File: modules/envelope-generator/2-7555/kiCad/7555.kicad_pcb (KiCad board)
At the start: 2 copper layers, 81 x 111 mm, 87 parts, among them J1 JUMPER_BUS_GATE, J2 PWR, Q1 BC547, Q2 BC547, Q3 BC547, SW1 SW_SPDT, U1 TL074, U2 ICM7555xP

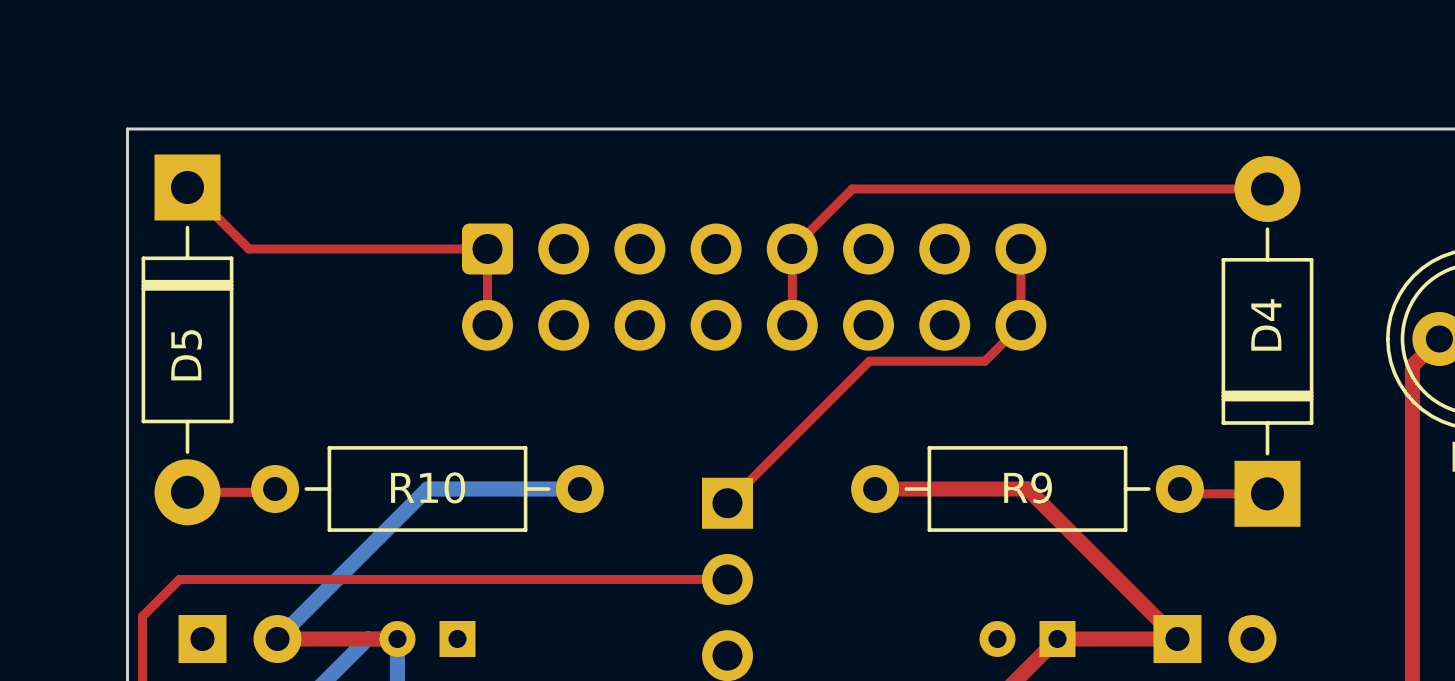
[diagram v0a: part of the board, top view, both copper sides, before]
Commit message: update XFO and 7555 ADSR, update status in readme
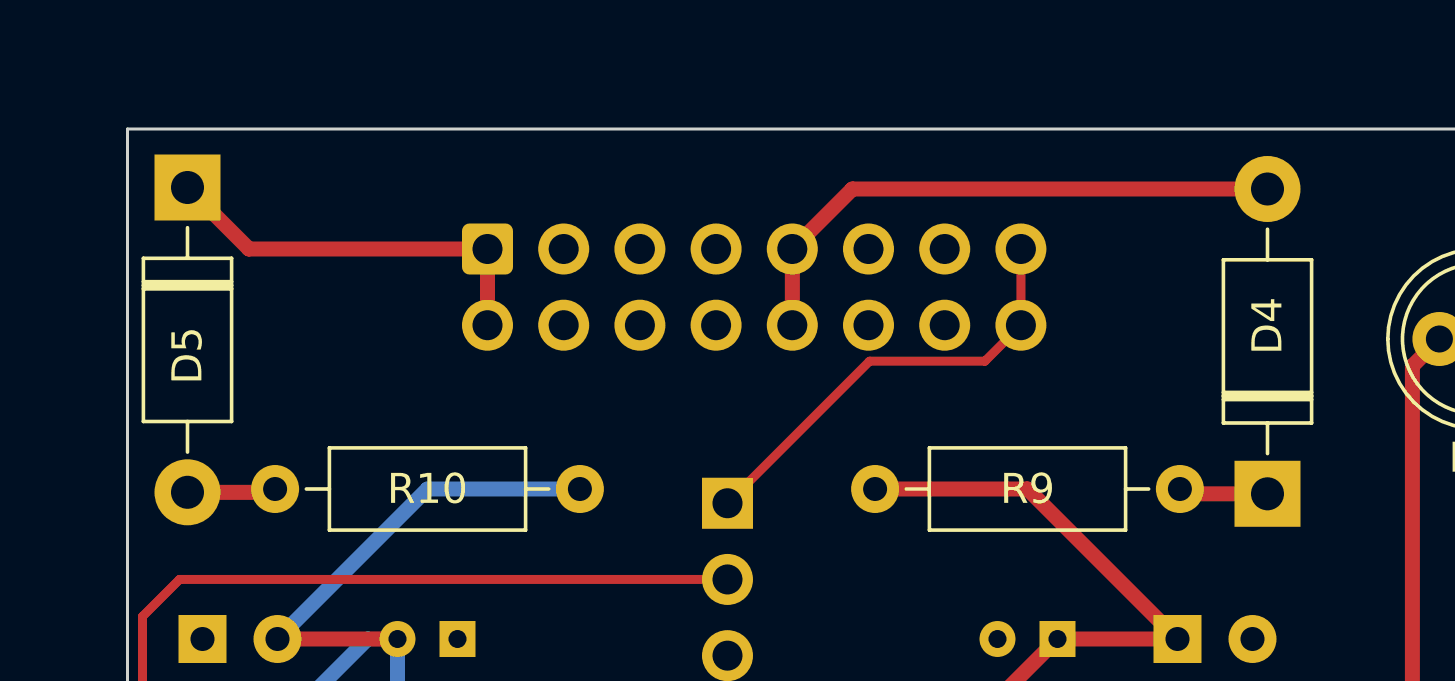
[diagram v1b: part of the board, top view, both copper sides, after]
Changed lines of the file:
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@@
 		(start 62 56.54)
 		(end 62 54)
-		(width 0.3)
+		(width 0.5)
 		(layer "F.Cu")
 		(net 10)
@@
 		(start 54.05 54)
 		(end 52 51.95)
-		(width 0.3)
+		(width 0.5)
 		(layer "F.Cu")
 		(net 10)
@@
 		(start 62 54)
 		(end 54.05 54)
-		(width 0.3)
+		(width 0.5)
 		(layer "F.Cu")
 		(net 10)
@@
 		(start 54.81 62.11)
 		(end 54.92 62)
-		(width 0.3)
+		(width 0.5)
 		(layer "F.Cu")
 		(net 11)
@@
 		(start 52 62.11)
 		(end 54.81 62.11)
-		(width 0.3)
+		(width 0.5)
 		(layer "F.Cu")
 		(net 11)
@@
 		(start 72.16 54)
 		(end 74.16 52)
-		(width 0.3)
+		(width 0.5)
 		(layer "F.Cu")
 		(net 52)
@@
 		(start 72.16 56.54)
 		(end 72.16 54)
-		(width 0.3)
+		(width 0.5)
 		(layer "F.Cu")
 		(net 52)
@@
 		(start 74.16 52)
 		(end 88 52)
-		(width 0.3)
+		(width 0.5)
 		(layer "F.Cu")
 		(net 52)
@@
 		(start 88 62.16)
 		(end 85.24 62.16)
-		(width 0.3)
+		(width 0.5)
 		(layer "F.Cu")
 		(net 53)
@@
 		(start 85.24 62.16)
 		(end 85.08 62)
-		(width 0.3)
+		(width 0.5)
 		(layer "F.Cu")
 		(net 53)

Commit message: update components, PCB 3320 and design
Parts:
- added H15: PinHeader_01x02, Synth:PinSocket_1x02_P2.54mm_Vertical, F.Cu at (53.0, 120.0)
- added H16: PinSocket_01x02, Synth:PinHeader_1x02_P2.54mm_Vertical, B.Cu at (94.0, 120.0)
- C10, C9: moved to B.Cu
- moved C9 68.9 mm to (52.5, 131.2)
- moved C10 51.9 mm to (52.5, 125.0), turned to 0 degrees
- moved TP11 14.8 mm to (58.8, 145.5)
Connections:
- C10 pad 1: Net-(SW1-A) -> Net-(H15B-Pin_2)
- C9 pad 1: Net-(SW1-C) -> Net-(H15A-Pin_1)
- SW1 pad 1: Net-(SW1-A) -> Net-(H16B-Pin_2)
- SW1 pad 3: Net-(SW1-C) -> Net-(H16A-Pin_1)
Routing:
- net Net-(H16A-Pin_1): track 0.00 -> 24.6 mm
- net Net-(H16B-Pin_2): track 0.00 -> 14.1 mm
- net Net-(H15A-Pin_1): track 0.00 -> 12.6 mm
- net Net-(H15B-Pin_2): track 0.00 -> 8.70 mm
- net Net-(H2C-Pin_3): track 31.8 -> 35.2 mm
- net Net-(SW1-C): track 3.30 -> 0.00 mm
- net Net-(SW1-A): track 3.30 -> 0.00 mm
- net -12V: track 95.7 -> 92.6 mm
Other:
- board text added: "REV.1"

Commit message: final versions of PCB for modules
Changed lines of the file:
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@@
 		(grid_origin 50 50)
 		(pcbplotparams
-			(layerselection 0x00010fc_ffffffff)
+			(layerselection 0x00410fc_ffffffff)
 			(plot_on_all_layers_selection 0x0000000_00000000)
 			(disableapertmacros no)
-			(usegerberextensions no)
-			(usegerberattributes yes)
-			(usegerberadvancedattributes yes)
-			(creategerberjobfile yes)
+			(usegerberextensions yes)
+			(usegerberattributes no)
+			(usegerberadvancedattributes no)
+			(creategerberjobfile no)
 			(dashed_line_dash_ratio 12.000000)
 			(dashed_line_gap_ratio 3.000000)
@@
 			(psa4output no)
 			(plotreference yes)
-			(plotvalue yes)
+			(plotvalue no)
 			(plotfptext yes)
 			(plotinvisibletext no)
 			(sketchpadsonfab no)
-			(subtractmaskfromsilk no)
+			(subtractmaskfromsilk yes)
 			(outputformat 1)
 			(mirror no)
-			(drillshape 1)
+			(drillshape 0)
 			(scaleselection 1)
-			(outputdirectory "")
+			(outputdirectory "../gerbers/")
 		)
 	)
@@
 	)
 	(gr_text "REV.1"
-		(at 130 90.25 90)
+		(at 130 95 90)
 		(layer "F.SilkS")
 		(effects
@@
 	)
 	(gr_text "ADSR Envelope Generator\nBased on 7555 Timer"
-		(at 129 102.5 90)
+		(at 129 106 90)
 		(layer "F.SilkS")
 		(effects
 			(font
-				(size 1 1)
+				(size 1.4 1.4)
 				(thickness 0.15)
 			)
